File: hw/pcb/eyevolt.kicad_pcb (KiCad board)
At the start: 4 copper layers, 122.3 x 48.8 mm, 28 parts, among them J1 Conn_02x10_Odd_Even, J2 Conn_01x15, J3 Conn_01x15, U1 Pico, U2 MCP6L04x-xSL, U3 MCP6L04x-xSL, U4 74HCT4051, U5 MCP6L04x-xSL, U6 MCP6L04x-xSL, U7 74HCT4051

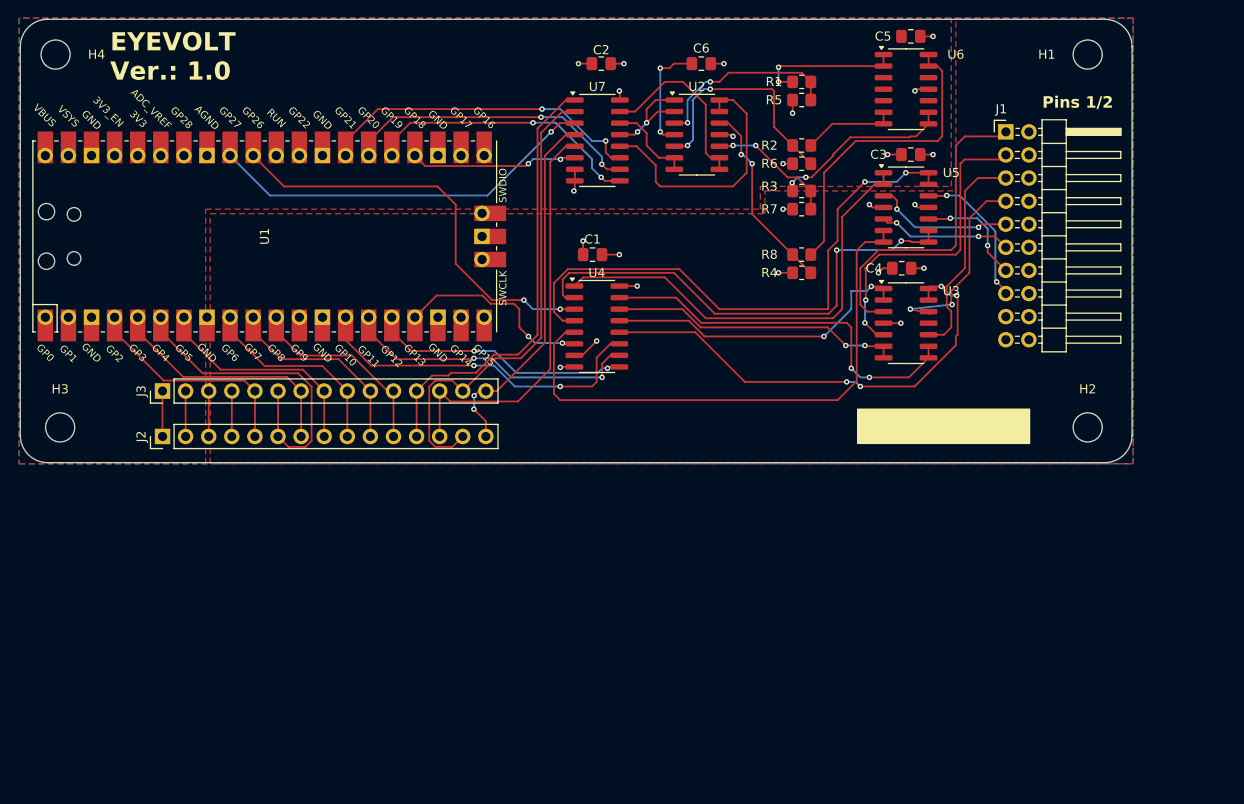
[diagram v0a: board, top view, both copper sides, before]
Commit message: Fix schematic errors - Regenerate a PCB for version 1.1
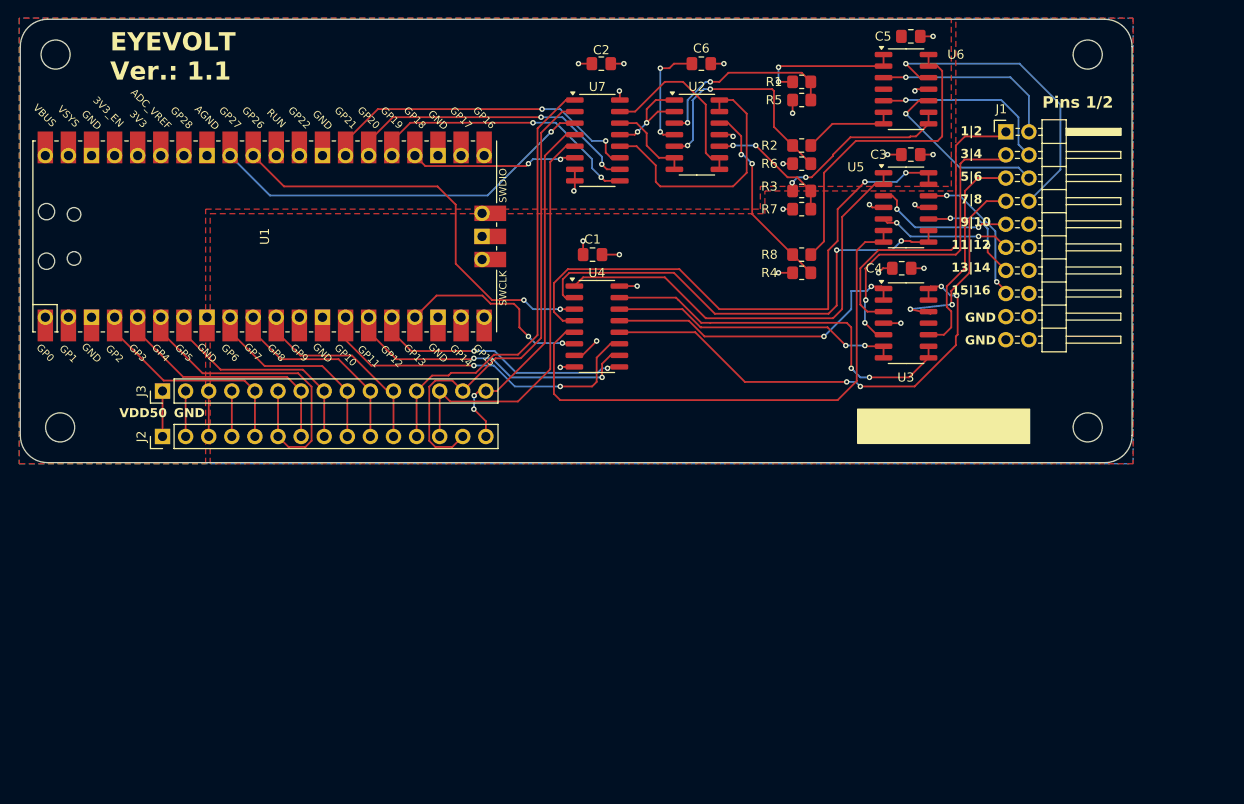
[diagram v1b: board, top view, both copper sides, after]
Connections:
- J1 pad 2: V55IN0 -> V50IN0
- J1 pad 4: V55IN1 -> V50IN1
- J1 pad 6: V55IN2 -> V50IN2
- J1 pad 8: V55IN3 -> V50IN3
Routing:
- net V50IN3: track 0.00 -> 34.1 mm, vias 0 -> 1
- net V50IN0: track 0.01 -> 20.8 mm, vias 0 -> 1
- net V50IN1: track 0.00 -> 20.3 mm, vias 0 -> 1
- net V50IN2: track 0.00 -> 19.6 mm, vias 0 -> 1
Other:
- board text added: "11|12"
- board text added: "13|14"
- board text added: "15|16"
- board text added: "1|2"
- board text added: "3|4"
- board text added: "5|6"
- board text added: "7|8"
- board text added: "9|10"
- board text added: "EYEVOLT Ver.: 1.1"
- board text added: "GND"
- board text added: "VDD50"
- board text removed: "EYEVOLT Ver.: 1.0"

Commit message: Start new 2.0 version with 8 PWM-based DAC
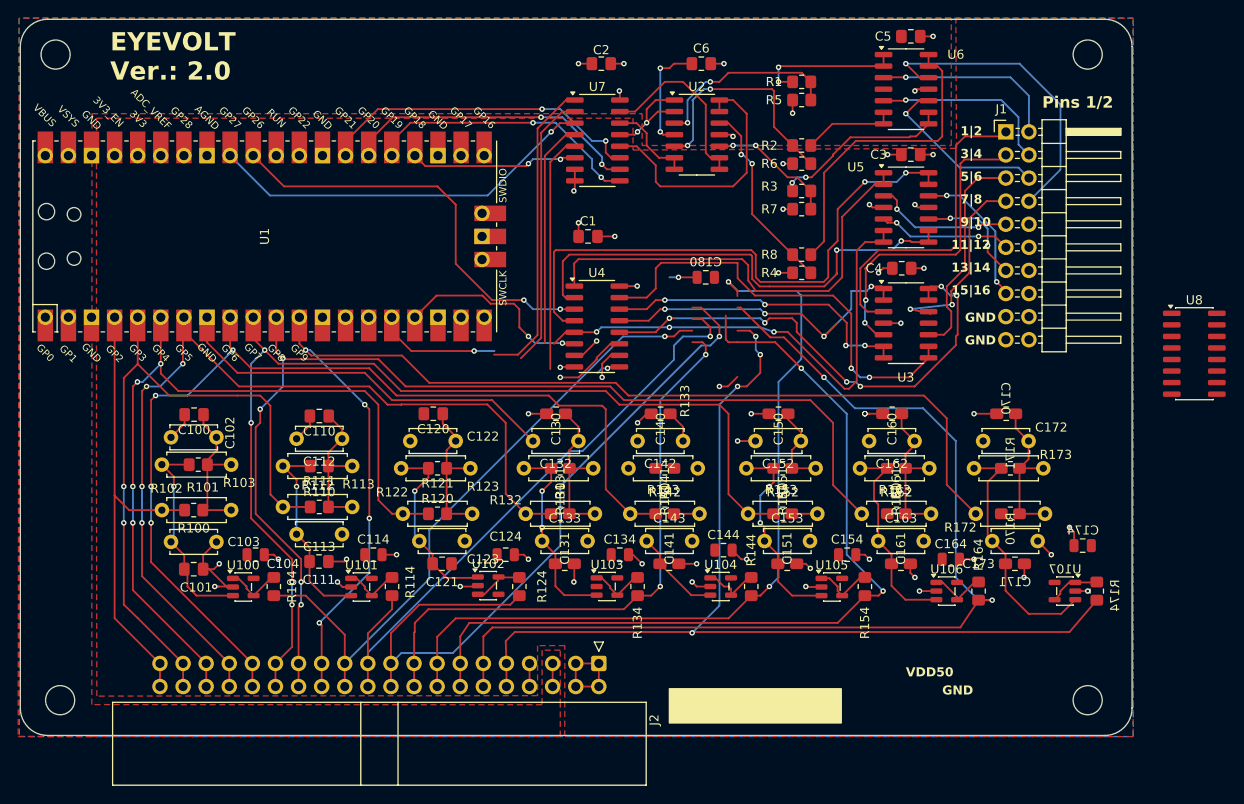
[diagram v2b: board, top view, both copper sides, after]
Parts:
- removed J3: Conn_01x15, Connector_PinHeader_2.54mm:PinHeader_1x15_P2.54mm_Vertical
- added C100: 1uF, Capacitor_SMD:C_0805_2012Metric_Pad1.18x1.45mm_HandSolder, F.Cu at (53.2, 89.6)
- added C101: 1uF, Capacitor_SMD:C_0805_2012Metric_Pad1.18x1.45mm_HandSolder, F.Cu at (53.2, 106.6)
- added C102: DNP 1uF TH ALT, Capacitor_THT:C_Disc_D5.0mm_W2.5mm_P5.00mm, F.Cu at (55.7, 92.1)
- added C103: DNP 1uF TH ALT, Capacitor_THT:C_Disc_D5.0mm_W2.5mm_P5.00mm, F.Cu at (50.7, 103.6)
- added C104: 100nF, Capacitor_SMD:C_0805_2012Metric, F.Cu at (60.0, 105.0)
- added C110: 1uF, Capacitor_SMD:C_0805_2012Metric_Pad1.18x1.45mm_HandSolder, F.Cu at (67.0, 89.8)
- added C111: 1uF, Capacitor_SMD:C_0805_2012Metric_Pad1.18x1.45mm_HandSolder, F.Cu at (67.0, 105.8)
- added C112: DNP 1uF TH ALT, Capacitor_THT:C_Disc_D5.0mm_W2.5mm_P5.00mm, F.Cu at (69.5, 92.2)
- added C113: DNP 1uF TH ALT, Capacitor_THT:C_Disc_D5.0mm_W2.5mm_P5.00mm, F.Cu at (64.5, 102.8)
- added C114: 100nF, Capacitor_SMD:C_0805_2012Metric, F.Cu at (73.0, 105.0)
- added C120: 1uF, Capacitor_SMD:C_0805_2012Metric_Pad1.18x1.45mm_HandSolder, F.Cu at (79.5, 89.5)
- added C121: 1uF, Capacitor_SMD:C_0805_2012Metric_Pad1.18x1.45mm_HandSolder, F.Cu at (80.5, 106.0)
- added C122: DNP 1uF TH ALT, Capacitor_THT:C_Disc_D5.0mm_W2.5mm_P5.00mm, F.Cu at (82.0, 92.5)
- added C123: DNP 1uF TH ALT, Capacitor_THT:C_Disc_D5.0mm_W2.5mm_P5.00mm, F.Cu at (78.0, 103.5)
- added C124: 100nF, Capacitor_SMD:C_0805_2012Metric, F.Cu at (87.5, 105.0)
- added C130: 1uF, Capacitor_SMD:C_0805_2012Metric_Pad1.18x1.45mm_HandSolder, F.Cu at (93.0, 89.5)
- added C131: 1uF, Capacitor_SMD:C_0805_2012Metric_Pad1.18x1.45mm_HandSolder, F.Cu at (94.0, 106.0)
- added C132: DNP 1uF TH ALT, Capacitor_THT:C_Disc_D5.0mm_W2.5mm_P5.00mm, F.Cu at (95.5, 92.5)
- added C133: DNP 1uF TH ALT, Capacitor_THT:C_Disc_D5.0mm_W2.5mm_P5.00mm, F.Cu at (91.5, 103.5)
- added C134: 100nF, Capacitor_SMD:C_0805_2012Metric, F.Cu at (100.0, 105.0)
- added C140: 1uF, Capacitor_SMD:C_0805_2012Metric_Pad1.18x1.45mm_HandSolder, F.Cu at (104.5, 89.5)
- added C141: 1uF, Capacitor_SMD:C_0805_2012Metric_Pad1.18x1.45mm_HandSolder, F.Cu at (105.5, 106.0)
- added C142: DNP 1uF TH ALT, Capacitor_THT:C_Disc_D5.0mm_W2.5mm_P5.00mm, F.Cu at (107.0, 92.5)
- added C143: DNP 1uF TH ALT, Capacitor_THT:C_Disc_D5.0mm_W2.5mm_P5.00mm, F.Cu at (103.0, 103.5)
- added C144: 100nF, Capacitor_SMD:C_0805_2012Metric, F.Cu at (111.5, 104.5)
- added C150: 1uF, Capacitor_SMD:C_0805_2012Metric_Pad1.18x1.45mm_HandSolder, F.Cu at (117.5, 89.5)
- added C151: 1uF, Capacitor_SMD:C_0805_2012Metric_Pad1.18x1.45mm_HandSolder, F.Cu at (118.5, 106.0)
- added C152: DNP 1uF TH ALT, Capacitor_THT:C_Disc_D5.0mm_W2.5mm_P5.00mm, F.Cu at (120.0, 92.5)
- added C153: DNP 1uF TH ALT, Capacitor_THT:C_Disc_D5.0mm_W2.5mm_P5.00mm, F.Cu at (116.0, 103.5)
- added C154: 100nF, Capacitor_SMD:C_0805_2012Metric, F.Cu at (125.0, 105.0)
- added C160: 1uF, Capacitor_SMD:C_0805_2012Metric_Pad1.18x1.45mm_HandSolder, F.Cu at (130.0, 89.5)
- added C161: 1uF, Capacitor_SMD:C_0805_2012Metric_Pad1.18x1.45mm_HandSolder, F.Cu at (131.0, 106.0)
- added C162: DNP 1uF TH ALT, Capacitor_THT:C_Disc_D5.0mm_W2.5mm_P5.00mm, F.Cu at (132.5, 92.5)
- added C163: DNP 1uF TH ALT, Capacitor_THT:C_Disc_D5.0mm_W2.5mm_P5.00mm, F.Cu at (128.5, 103.5)
- added C164: 100nF, Capacitor_SMD:C_0805_2012Metric, F.Cu at (136.4, 105.5)
- added C170: 1uF, Capacitor_SMD:C_0805_2012Metric_Pad1.18x1.45mm_HandSolder, F.Cu at (142.5, 89.5)
- added C171: 1uF, Capacitor_SMD:C_0805_2012Metric_Pad1.18x1.45mm_HandSolder, F.Cu at (143.5, 106.0)
- added C172: DNP 1uF TH ALT, Capacitor_THT:C_Disc_D5.0mm_W2.5mm_P5.00mm, F.Cu at (145.0, 92.5)
- added C173: DNP 1uF TH ALT, Capacitor_THT:C_Disc_D5.0mm_W2.5mm_P5.00mm, F.Cu at (141.0, 103.5)
- added C174: 100nF, Capacitor_SMD:C_0805_2012Metric, F.Cu at (150.9, 104.0)
- added C180: 100nF, Capacitor_SMD:C_0805_2012Metric, F.Cu at (109.5, 74.5)
- added R100: 10k, Resistor_SMD:R_0805_2012Metric_Pad1.20x1.40mm_HandSolder, F.Cu at (53.2, 100.1)
- added R101: 10k, Resistor_SMD:R_0805_2012Metric_Pad1.20x1.40mm_HandSolder, F.Cu at (53.7, 95.1)
- added R102: DNP 10k TH ALT, Resistor_THT:R_Axial_DIN0207_L6.3mm_D2.5mm_P7.62mm_Horizontal, F.Cu at (49.7, 100.1)
- added R103: DNP 10k TH ALT, Resistor_THT:R_Axial_DIN0207_L6.3mm_D2.5mm_P7.62mm_Horizontal, F.Cu at (57.3, 95.1)
- added R104: 0R OUT_LINK, Resistor_SMD:R_0805_2012Metric_Pad1.20x1.40mm_HandSolder, F.Cu at (62.0, 108.5)
- added R110: 10k, Resistor_SMD:R_0805_2012Metric_Pad1.20x1.40mm_HandSolder, F.Cu at (67.0, 99.8)
- added R111: 10k, Resistor_SMD:R_0805_2012Metric_Pad1.20x1.40mm_HandSolder, F.Cu at (67.0, 95.2)
- added R112: DNP 10k TH ALT, Resistor_THT:R_Axial_DIN0207_L6.3mm_D2.5mm_P7.62mm_Horizontal, F.Cu at (63.0, 99.8)
- added R113: DNP 10k TH ALT, Resistor_THT:R_Axial_DIN0207_L6.3mm_D2.5mm_P7.62mm_Horizontal, F.Cu at (70.6, 95.2)
- added R114: 0R OUT_LINK, Resistor_SMD:R_0805_2012Metric_Pad1.20x1.40mm_HandSolder, F.Cu at (75.0, 108.5)
- added R120: 10k, Resistor_SMD:R_0805_2012Metric_Pad1.20x1.40mm_HandSolder, F.Cu at (80.0, 100.5)
- added R121: 10k, Resistor_SMD:R_0805_2012Metric_Pad1.20x1.40mm_HandSolder, F.Cu at (80.0, 95.5)
- added R122: DNP 10k TH ALT, Resistor_THT:R_Axial_DIN0207_L6.3mm_D2.5mm_P7.62mm_Horizontal, F.Cu at (76.2, 100.5)
- added R123: DNP 10k TH ALT, Resistor_THT:R_Axial_DIN0207_L6.3mm_D2.5mm_P7.62mm_Horizontal, F.Cu at (83.6, 95.5)
- added R124: 0R OUT_LINK, Resistor_SMD:R_0805_2012Metric_Pad1.20x1.40mm_HandSolder, F.Cu at (89.0, 108.5)
- added R130: 10k, Resistor_SMD:R_0805_2012Metric_Pad1.20x1.40mm_HandSolder, F.Cu at (93.5, 100.5)
- added R131: 10k, Resistor_SMD:R_0805_2012Metric_Pad1.20x1.40mm_HandSolder, F.Cu at (93.5, 95.5)
- added R132: DNP 10k TH ALT, Resistor_THT:R_Axial_DIN0207_L6.3mm_D2.5mm_P7.62mm_Horizontal, F.Cu at (89.7, 100.5)
- added R133: DNP 10k TH ALT, Resistor_THT:R_Axial_DIN0207_L6.3mm_D2.5mm_P7.62mm_Horizontal, F.Cu at (97.1, 95.5)
- added R134: 0R OUT_LINK, Resistor_SMD:R_0805_2012Metric_Pad1.20x1.40mm_HandSolder, F.Cu at (102.0, 108.5)
- added R140: 10k, Resistor_SMD:R_0805_2012Metric_Pad1.20x1.40mm_HandSolder, F.Cu at (105.0, 100.5)
- added R141: 10k, Resistor_SMD:R_0805_2012Metric_Pad1.20x1.40mm_HandSolder, F.Cu at (105.0, 95.5)
- added R142: DNP 10k TH ALT, Resistor_THT:R_Axial_DIN0207_L6.3mm_D2.5mm_P7.62mm_Horizontal, F.Cu at (101.2, 100.5)
- added R143: DNP 10k TH ALT, Resistor_THT:R_Axial_DIN0207_L6.3mm_D2.5mm_P7.62mm_Horizontal, F.Cu at (108.6, 95.5)
- added R144: 0R OUT_LINK, Resistor_SMD:R_0805_2012Metric_Pad1.20x1.40mm_HandSolder, F.Cu at (114.5, 108.5)
- added R150: 10k, Resistor_SMD:R_0805_2012Metric_Pad1.20x1.40mm_HandSolder, F.Cu at (118.0, 100.5)
- added R151: 10k, Resistor_SMD:R_0805_2012Metric_Pad1.20x1.40mm_HandSolder, F.Cu at (118.0, 95.5)
- added R152: DNP 10k TH ALT, Resistor_THT:R_Axial_DIN0207_L6.3mm_D2.5mm_P7.62mm_Horizontal, F.Cu at (114.2, 100.5)
- added R153: DNP 10k TH ALT, Resistor_THT:R_Axial_DIN0207_L6.3mm_D2.5mm_P7.62mm_Horizontal, F.Cu at (121.6, 95.5)
- added R154: 0R OUT_LINK, Resistor_SMD:R_0805_2012Metric_Pad1.20x1.40mm_HandSolder, F.Cu at (127.0, 108.5)
- added R160: 10k, Resistor_SMD:R_0805_2012Metric_Pad1.20x1.40mm_HandSolder, F.Cu at (130.5, 100.5)
- added R161: 10k, Resistor_SMD:R_0805_2012Metric_Pad1.20x1.40mm_HandSolder, F.Cu at (130.5, 95.5)
- added R162: DNP 10k TH ALT, Resistor_THT:R_Axial_DIN0207_L6.3mm_D2.5mm_P7.62mm_Horizontal, F.Cu at (126.7, 100.5)
- added R163: DNP 10k TH ALT, Resistor_THT:R_Axial_DIN0207_L6.3mm_D2.5mm_P7.62mm_Horizontal, F.Cu at (134.1, 95.5)
- added R164: 0R OUT_LINK, Resistor_SMD:R_0805_2012Metric_Pad1.20x1.40mm_HandSolder, F.Cu at (139.5, 109.0)
- added R170: 10k, Resistor_SMD:R_0805_2012Metric_Pad1.20x1.40mm_HandSolder, F.Cu at (143.0, 100.5)
- added R171: 10k, Resistor_SMD:R_0805_2012Metric_Pad1.20x1.40mm_HandSolder, F.Cu at (143.0, 95.5)
- added R172: DNP 10k TH ALT, Resistor_THT:R_Axial_DIN0207_L6.3mm_D2.5mm_P7.62mm_Horizontal, F.Cu at (139.2, 100.5)
- added R173: DNP 10k TH ALT, Resistor_THT:R_Axial_DIN0207_L6.3mm_D2.5mm_P7.62mm_Horizontal, F.Cu at (146.6, 95.5)
- added R174: 0R OUT_LINK, Resistor_SMD:R_0805_2012Metric_Pad1.20x1.40mm_HandSolder, F.Cu at (152.5, 109.0)
- added U100: OPA316QDBVTQ1, Package_TO_SOT_SMD:SOT-23-5, F.Cu at (58.6, 108.6)
- added U101: OPA316QDBVTQ1, Package_TO_SOT_SMD:SOT-23-5, F.Cu at (71.6, 108.6)
- added U102: OPA316QDBVTQ1, Package_TO_SOT_SMD:SOT-23-5, F.Cu at (85.6, 108.4)
- added U103: OPA316QDBVTQ1, Package_TO_SOT_SMD:SOT-23-5, F.Cu at (98.6, 108.5)
- added U104: OPA316QDBVTQ1, Package_TO_SOT_SMD:SOT-23-5, F.Cu at (111.1, 108.5)
- added U105: OPA316QDBVTQ1, Package_TO_SOT_SMD:SOT-23-5, F.Cu at (123.4, 108.5)
- added U106: OPA316QDBVTQ1, Package_TO_SOT_SMD:SOT-23-5, F.Cu at (136.0, 109.0)
- added U107: OPA316QDBVTQ1, Package_TO_SOT_SMD:SOT-23-5, F.Cu at (149.0, 109.0)
- added U8: 74HCT4051 DAC_FB_MUX, Package_SO:SOIC-16_3.9x9.9mm_P1.27mm, F.Cu at (163.2, 82.9)
- J2: value Conn_01x15 -> DAC_PWM_DAC_OUT_2x20; footprint Connector_PinHeader_2.54mm:PinHeader_1x15_P2.54mm_Vertical -> Connector_IDC:IDC-Header_2x20_P2.54mm_Horizontal
- moved J2 54.1 mm to (97.7, 117.0), turned to -90 degrees
- moved H2 30.0 mm to (151.5, 121.0)
- moved H3 30.0 mm to (38.5, 121.0)
- moved C1 2.06 mm to (96.5, 70.0)
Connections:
- J2 pad 1: /VDD50 -> GND
- J2 pad 10: /WAIT -> /DAC_OUT7
- J2 pad 11: /INT -> /DAC_OUT6
- J2 pad 12: /Y+ -> /DAC_OUT6
- J2 pad 13: /Y- -> /DAC_OUT5
- J2 pad 14: /X- -> /DAC_OUT5
- J2 pad 15: /X+ -> /DAC_OUT4
- J2 pad 3: /3Vo -> GND
- J2 pad 4: /LITE -> GND
- J2 pad 5: /SCK -> /VDD50
- J2 pad 6: /MISO -> /VDD50
- J2 pad 7: /MOSI -> /VDD33
- J2 pad 8: /CS -> /VDD33
- J2 pad 9: /RST -> /DAC_OUT7
- U1 pad 10: /WAIT -> /DAC_PWM5
- U1 pad 11: /INT -> /DAC_PWM6
- U1 pad 12: unconnected-(U1-GPIO9-Pad12) -> /DAC_PWM7
- U1 pad 19: unconnected-(U1-GPIO14-Pad19)_1 -> /DACMUX_S0
- U1 pad 20: unconnected-(U1-GPIO15-Pad20) -> /DACMUX_S1
- U1 pad 21: unconnected-(U1-GPIO16-Pad21)_1 -> /DACMUX_S2
- U1 pad 22: unconnected-(U1-GPIO17-Pad22) -> /DACMUX_EB
- U1 pad 31: /MUX0_A -> /MON_ADC_A
- U1 pad 32: /MUX1_A -> /DAC_FB_A
- U1 pad 4: /SCK -> /DAC_PWM0
- U1 pad 5: /MOSI -> /DAC_PWM1
- U1 pad 6: /MISO -> /DAC_PWM2
- U1 pad 7: /CS -> /DAC_PWM3
- U1 pad 9: /RST -> /DAC_PWM4
- U4 pad 3: /MUX0_A -> /MUX0_A_TO_MUX1
- U7 pad 1: /Y+ -> /MUX0_A_TO_MUX1
- U7 pad 2: /X- -> /MUX1_SPARE_A6
- U7 pad 3: /MUX1_A -> /MON_ADC_A
- U7 pad 4: /X+ -> /MUX1_SPARE_A7
- U7 pad 5: /Y- -> /MUX1_SPARE_A5
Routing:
- net /DAC_PWM7: track 0.00 -> 131.9 mm, vias 0 -> 4
- net GND: track 31.8 -> 155.7 mm, vias 16 -> 48
- net /DAC_PWM6: track 0.00 -> 119.1 mm, vias 0 -> 4
- net /DAC_OUT6: track 0.00 -> 113.6 mm, vias 0 -> 2
- net /DAC_PWM5: track 0.00 -> 113.0 mm, vias 0 -> 4
- net /DAC_OUT7: track 0.00 -> 110.8 mm, vias 0 -> 4
- net /DAC_PWM4: track 0.00 -> 110.2 mm, vias 0 -> 4
- net /DAC_PWM3: track 0.00 -> 103.9 mm, vias 0 -> 4
- net /DAC_OUT5: track 0.00 -> 94.7 mm, vias 0 -> 2
- net (no net): track 0.00 -> 89.1 mm, vias 0 -> 3
- net /DAC_PWM2: track 0.00 -> 88.6 mm, vias 0 -> 4
- net /DAC_OUT4: track 0.00 -> 88.3 mm, vias 0 -> 2
- net /DAC_OUT2: track 0.00 -> 81.5 mm, vias 0 -> 1
- net /DAC_PWM1: track 0.00 -> 75.2 mm, vias 0 -> 2
- net /DAC_OUT0: track 0.00 -> 71.8 mm, vias 0 -> 1
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- added copper zone on F.Cu, net /VDD33
- removed copper zone on F.Cu, net GND
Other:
- board size 122.3 x 48.8 mm -> 122.3 x 78.8 mm
- board text added: "EYEVOLT Ver.: 2.0"
- board text removed: "EYEVOLT Ver.: 1.1"
